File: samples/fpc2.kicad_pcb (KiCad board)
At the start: 2 copper layers, 15 x 13.4 mm, 2 parts, among them J2 Conn_01x02_Pin

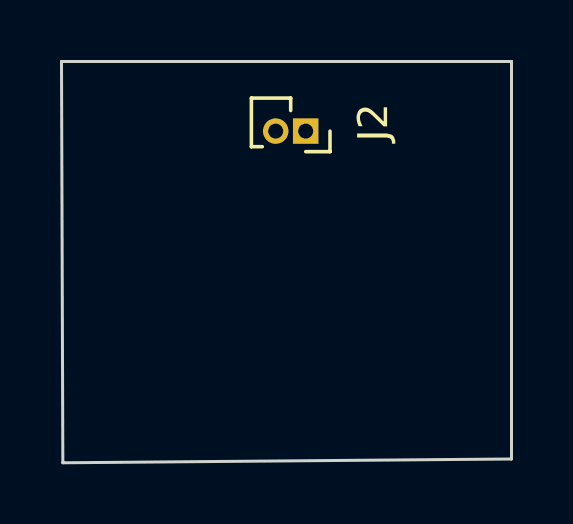
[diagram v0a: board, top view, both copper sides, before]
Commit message: Add coupler offsets and robust bend mapping
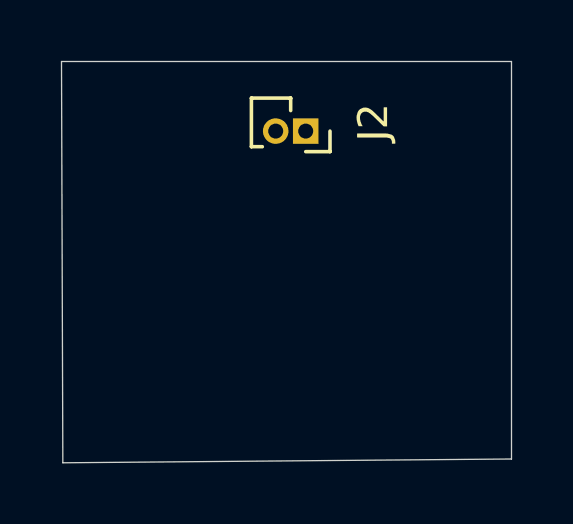
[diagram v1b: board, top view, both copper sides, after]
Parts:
- conn: footprint Kikakuka:CouplerMoving -> PCM_Kikakuka:CouplerMoving
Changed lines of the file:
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@@
 		)
 	)
-	(footprint "Kikakuka:CouplerMoving"
+	(footprint "PCM_Kikakuka:CouplerMoving"
 		(layer "F.Cu")
 		(at 98.64 85.52 180)
@@
 			)
 		)
-		(property "Description" ""
+		(property "Description" "Moving FreekiCAD alignment plane. Positions this PCB against a CouplerFixed footprint with the same reference. Z moves along the PCB surface normal; positive Offset moves on the PCB surface in the triangle direction; Tilt rotates around local X. Unitless lengths default to mm; mm/in/mil/um are supported."
 			(at 0 0 180)
 			(unlocked yes)
@@
 			)
 		)
-		(property "Z" "2.1mm"
+		(property "Z" "2.1 mm"
+			(at 0 0 180)
+			(unlocked yes)
+			(layer "F.Fab")
+			(hide yes)
+			(effects
+				(font
+					(size 1 1)
+					(thickness 0.15)
+				)
+			)
+		)
+		(property "Offset" "0 mm"
 			(at 0 0 180)
 			(unlocked yes)
@@
 		)
 		(fp_line
+			(start 0.25 -0.75)
+			(end 0 -0.5)
+			(stroke
+				(width 0.1)
+				(type default)
+			)
+			(layer "Cmts.User")
+		)
+		(fp_line
 			(start 0 0)
 			(end -1 -1)
+			(stroke
+				(width 0.1)
+				(type default)
+			)
+			(layer "Cmts.User")
+		)
+		(fp_line
+			(start 0 -0.5)
+			(end -0.25 -0.75)
+			(stroke
+				(width 0.1)
+				(type default)
+			)
+			(layer "Cmts.User")
+		)
+		(fp_line
+			(start 0 -1)
+			(end 0 -0.5)
+			(stroke
+				(width 0.1)
+				(type default)
+			)
+			(layer "Cmts.User")
+		)
+		(fp_line
+			(start -0.25 -0.75)
+			(end 0 -0.5)
 			(stroke
 				(width 0.1)
@@
 		(end 105.5 83.5)
 		(stroke
-			(width 0.1)
+			(width 0)
 			(type default)
 		)
@@
 		(end 90.5 83.5)
 		(stroke
-			(width 0.1)
+			(width 0)
 			(type default)
 		)
@@
 		(end 105.5 96.75)
 		(stroke
-			(width 0.1)
+			(width 0)
 			(type default)
 		)
@@
 		(end 90.544618 96.876526)
 		(stroke
-			(width 0.1)
+			(width 0)
 			(type default)
 		)

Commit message: Add KiCad placeholder model plugin
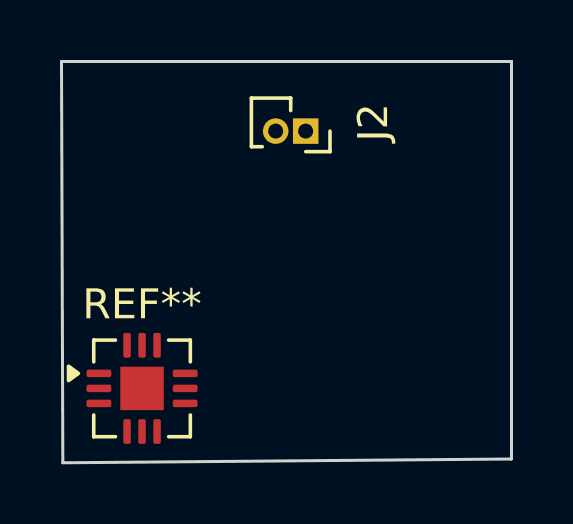
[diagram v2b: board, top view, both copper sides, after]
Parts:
- added REF**: QFN-12-1EP_3x3mm_P0.5mm_EP1.45x1.45mm, Package_DFN_QFN:QFN-12-1EP_3x3mm_P0.5mm_EP1.45x1.45mm, F.Cu at (93.2, 94.4)
